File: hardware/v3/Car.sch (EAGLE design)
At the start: 56 parts, among them IC1 PIC24FJ64GB204

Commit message: Started layout for v3.
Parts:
- removed 3V3: LM317, misc:LM317
- removed C1: 10u, rcl:C-USC1206
- removed C2, C3, C4, C5, PSB3: 100n, rcl:C-USC0805
- removed C7, PSB2: 1u, rcl:C-USC1206
- removed PSB1: 100u, SparkFun-Passives:CAP_POLC
- removed R15: 240, rcl:R-US_R0805
- removed R16: 390, rcl:R-US_R0805
- removed RL1, RL2: 2k, rcl:R-US_R0805
- removed RN1: 10k, rcl:R-US_R0805
- added C11: 100u, SparkFun-Passives:CAP_POLC
- added C12, C14, C16, C21: 10u, rcl:C-USC1206
- added C13, C15, C17, C22, C23, C24, C41: 100n, rcl:C-USC0805
- added CN1: (no value), SmslsTron-1:USBMINIB
- added D1: (no value), SmslsTron-1:SCHOTTKY-DIODESMA
- added IC2: LD117AS50TR, v-reg:LD117AS50TR
- added IC3: LD117AS33TR, v-reg:LD117AS33TR
- added JP5: (no value), SmslsTron-1:PINHD-1X4
- added R11, R22: 2k, rcl:R-US_R0805
- added R21: 10k, rcl:R-US_R0805
- added R23, R25: 1k, rcl:R-US_R0805
- added R24, R26: 100, rcl:R-US_R0805
- added S1: SWITCH-MOMENTARY-2SMD-4, SmslsTron-1:SWITCH-MOMENTARY-2SMD-4
- added T1, T2: (no value), SmslsTron-1:NPNSOT23
- added U$1: FUSE24X06, SmslsTron-1:FUSE24X06
- 11RS, 12RS, 21RS, 22RS: device resistor:R-US_R2512 -> resistor:R-US_R1210
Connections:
- removed net 12V: 1LDB.1, 1LDC.+, 2LDB.1, 2LDC.+, 3V3.VI, J1.1, MD1.VLOAD, MD2.VLOAD, PSB1.+, PSB2.1, PSB3.1
- removed net 3V3: 3V3.VO, C2.1, C3.1, C4.1, C5.1, C7.1, IC1.AVDD, IC1.VBAT, IC1.VDD@1, IC1.VDD@2, IC1.VUSB3V3, ICD.2, JP2.4, MOUTH.VCC, PWR.A, R15.2, RN1.1
- removed net 5V: 1LGB.1, 2LGB.1, MD1.VLOGIC, MD2.VLOGIC
- removed net A7: HB.A
- removed net D12/M2_P1: MD2.PHASE1
- removed net D13/M2_P2: MD2.PHASE2
- removed net D13/SCK: JP4.6
- removed net D14/M2_I0X: MD2.I01, MD2.I02
- removed net D15/M2_I1X: MD2.I11, MD2.I12
- removed net D4/M1_P2: MD1.PHASE2
- removed net D7/M1_I0X: MD1.I01, MD1.I02
- removed net D8/M1_I1X: MD1.I11, MD1.I12
- removed net DGND: MD1.GND1, MD1.GND2, MD1.GND3, MD1.GND4, MD2.GND1, MD2.GND2, MD2.GND3, MD2.GND4
- removed net M1_I00: IC1.SOSCO/SC0/RA4
- removed net M1_I10: IC1.TDO/CN34/RA8
- removed net M1_V1: MD1.VREF1
- removed net M1_V2: MD1.VREF2
- removed net M2_I00: IC1.TMS/CN36/RA10
- removed net M2_I10: IC1.AN11/RP17/CN9/RC1
- removed net M2_V1: MD2.VREF1
- removed net M2_V2: MD2.VREF2
- removed net MISO: MOUTH.SDO
- removed net MOSI: MOUTH.SDI
- removed net SCLK: MOUTH.SCLK
- new net +3V3: C16.1, C17.1, C22.1, C23.1, C24.1, C41.1, IC1.AVDD, IC1.VBAT, IC1.VDD@1, IC1.VDD@2, IC1.VUSB3V3, IC3.OUT, ICD.2, JP2.4, MOUTH.VCC, PWR.A, R21.1
- new net +5V: 1LGB.1, 2LGB.1, C14.1, C15.1, IC2.OUT, IC3.IN, JP2.5, JP5.1, MD1.VLOGIC, MD2.VLOGIC, R24.2, R26.2
- new net A4_PO: JP5.2, T1.E
- new net A5_PO: JP5.3, T2.E
- new net M1_I02: IC1.TDO/CN34/RA8, MD1.I02
- new net M1_I12: IC1.TDI/CN35/RA9, MD1.I12
- new net M2_I02: IC1.CN24/VBUS/RB6, MD2.I02
- new net M2_I12: IC1.RP7/CN23/RB7, MD2.I12
- new net N$12: R26.1, T2.C
- new net N$19: R23.2, T1.B
- new net N$3: D1.A, U$1.2
- new net N$7: R24.1, T1.C
- new net VIN_PRF: J1.1, U$1.1
- net /RST: now also R21.2, S1.1; no longer RN1.2
- net A4: now also R23.1
- net A5: now also R25.1
- net D10/M2_PWM2: now also MD2.VREF2
- net D11/MOSI: now also MOUTH.SDI
- net D12/MISO: now also MOUTH.SDO
- net D13/SCLK: now also HB.A, JP4.6, MOUTH.SCLK
- net D3/M1_P2: now also MD1.PHASE2
- net D4/M2_P1: now also MD2.PHASE1
- net D5/M1_PWM1: now also MD1.VREF1
- net D6/M1_PWM2: now also MD1.VREF2
- net D7/M2_P2: now also MD2.PHASE2
- net D9/M2_PWM1: now also MD2.VREF1
- net GND: now also C11.-, C12.2, C13.2, C14.2, C15.2, C16.2, C17.2, C21.2, C22.2, C23.2, C24.2, C41.2, IC2.ADJ, IC3.ADJ, JP5.4, MD1.GND1, MD1.GND2, MD1.GND3, MD1.GND4, MD2.GND1, MD2.GND2, MD2.GND3, MD2.GND4, R11.2, R22.2, S1.2; no longer C1.2, C2.2, C3.2, C4.2, C5.2, C7.2, PSB1.-, PSB2.2, PSB3.2, R16.1, RL1.2, RL2.2
- net M1_I01: now also IC1.SOSCO/SC0/RA4, MD1.I01; no longer IC1.TCK/CN33/RA7
- net M1_I11: now also IC1.TCK/CN33/RA7, MD1.I11; no longer IC1.TDI/CN35/RA9
- net M2_I01: now also IC1.TMS/CN36/RA10, MD2.I01; no longer IC1.AN9/RP15/CN11/RB15
- net M2_I11: now also IC1.AN9/RP15/CN11/RB15, MD2.I11; no longer IC1.AN12/RP18/CN10/RC2
- net N$20: now also R25.2, T2.B; no longer 3V3.ADJ, R15.1, R16.2
- net N$40: now also C21.1, IC1.VCAP; no longer C1.1
- net N$46: now also R22.1; no longer RL1.1
- net N$65: now also R11.1; no longer RL2.1
- net RFM_CS: now also IC1.AN12/RP18/CN10/RC2; no longer IC1.RP7/CN23/RB7
- net RFM_IRQ: now also IC1.AN11/RP17/CN9/RC1; no longer IC1.CN24/VBUS/RB6
- net VIN: now also 1LDB.1, 1LDC.+, 2LDB.1, 2LDC.+, C11.+, C12.1, C13.1, D1.C, IC2.IN, MD1.VLOAD, MD2.VLOAD

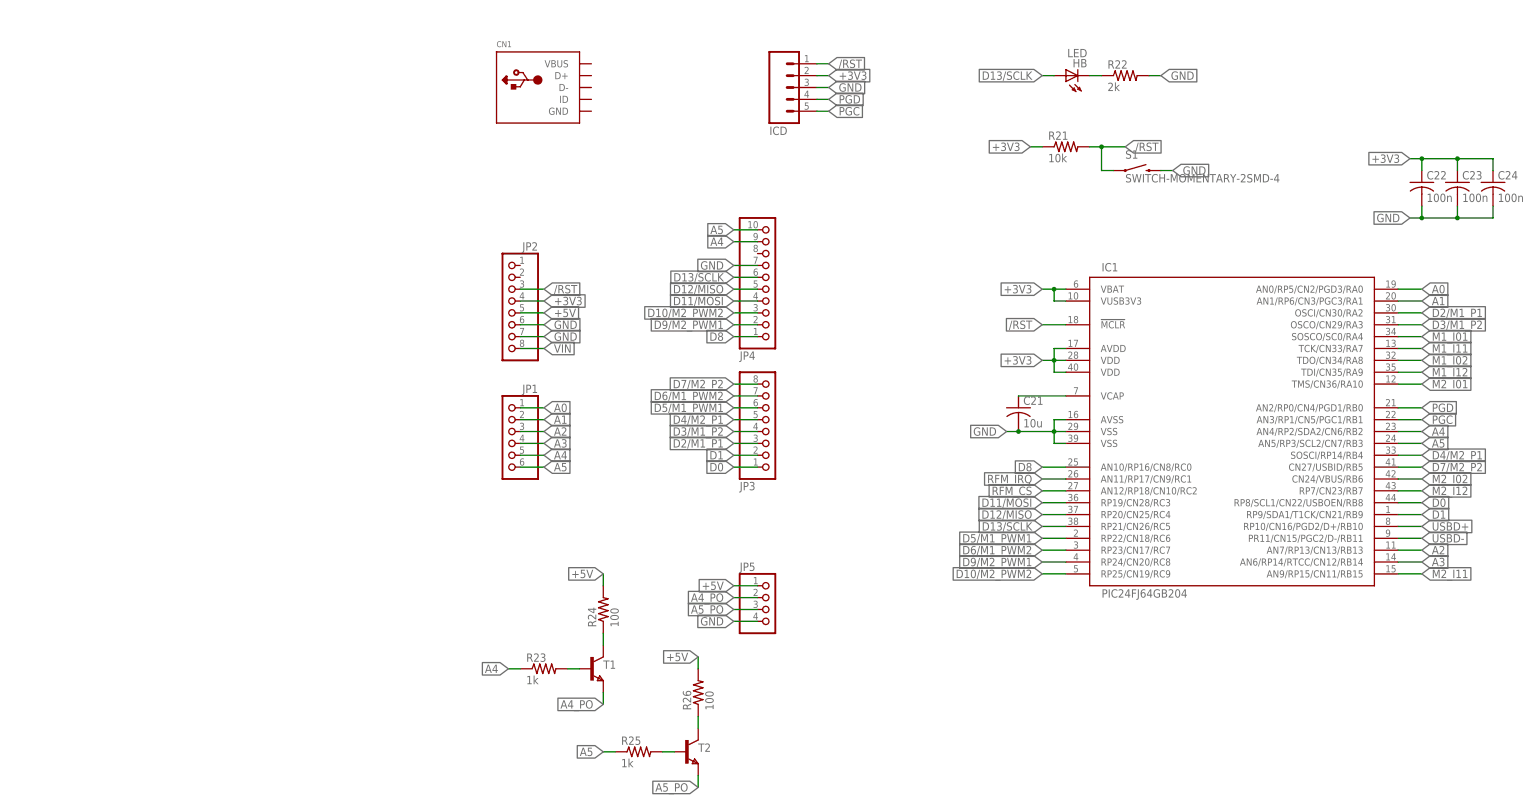
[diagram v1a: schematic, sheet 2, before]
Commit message: Continued working layout. Added USB components. Remapped some pins.
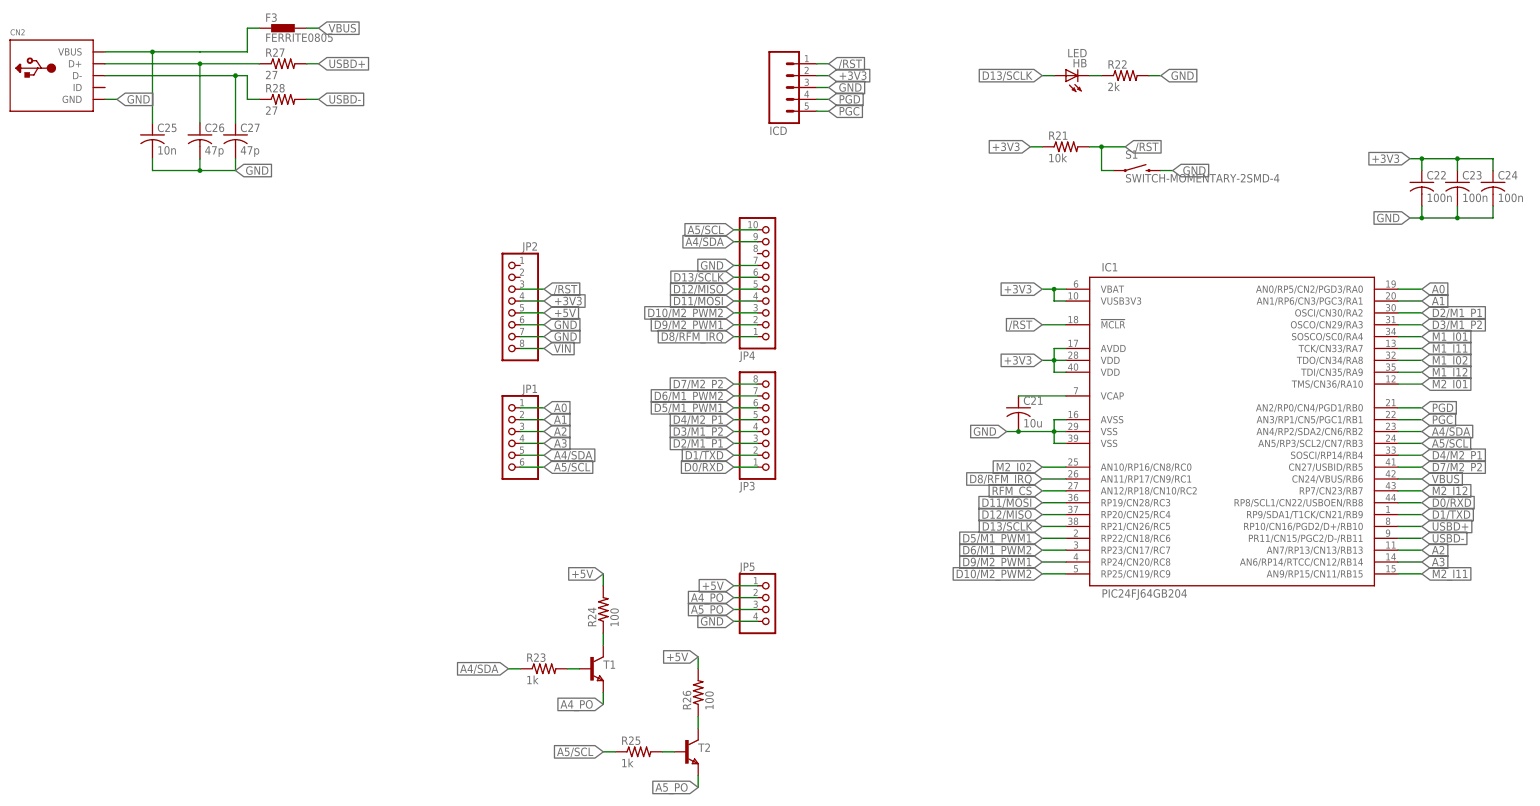
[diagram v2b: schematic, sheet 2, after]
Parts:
- removed CN1: (no value), SmslsTron-1:USBMINIB
- added C25: 10n, rcl:C-USC0805
- added C26, C27: 47p, rcl:C-USC0805
- added CN2: (no value), adafruit:USBMINIB
- added F3: FERRITE0805, SMSLS:FERRITE0805
- added R27, R28: 27, resistor:R-US_R0805
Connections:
- net A4 renamed A4/SDA
- net A5 renamed A5/SCL
- net D0 renamed D0/RXD
- net D1 renamed D1/TXD
- removed net D8: IC1.AN10/RP16/CN8/RC0, JP4.1
- removed net RFM_IRQ: IC1.AN11/RP17/CN9/RC1, MOUTH.NIRQ
- new net D8/RFM_IRQ: IC1.AN11/RP17/CN9/RC1, JP4.1, MOUTH.NIRQ
- new net N$21: C26.1, CN2.D+, R27.1
- new net N$22: C27.1, CN2.D-, R28.1
- new net VBUS: F3.2, IC1.CN24/VBUS/RB6
- new net VBUS-PRF: C25.1, CN2.VBUS, F3.1
- net GND: now also C25.2, C26.2, C27.2, CN2.GND
- net M2_I02: now also IC1.AN10/RP16/CN8/RC0; no longer IC1.CN24/VBUS/RB6
- net USBD+: now also R27.2
- net USBD-: now also R28.2

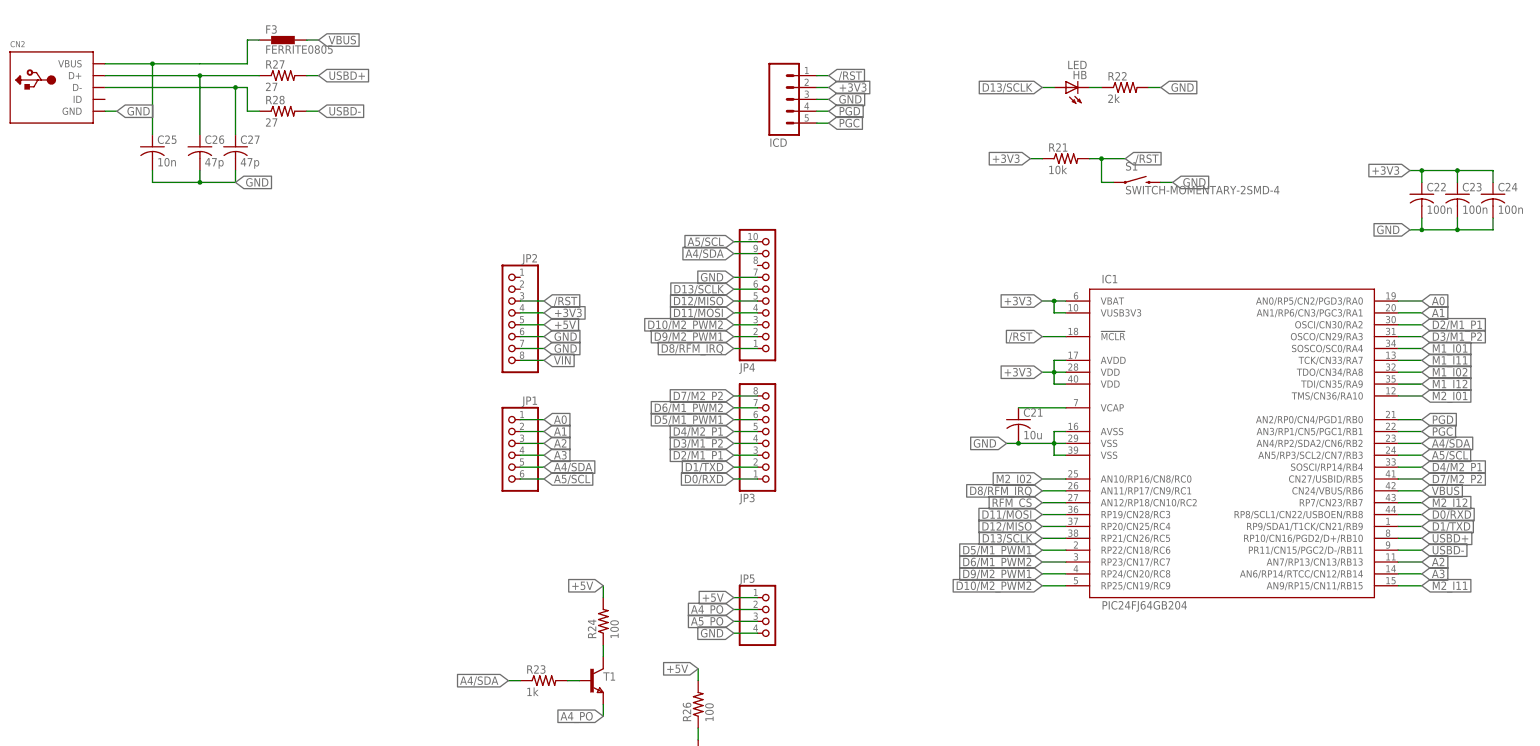
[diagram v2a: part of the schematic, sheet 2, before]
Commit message: More routing (~50% complete). Normalized/placed texts.
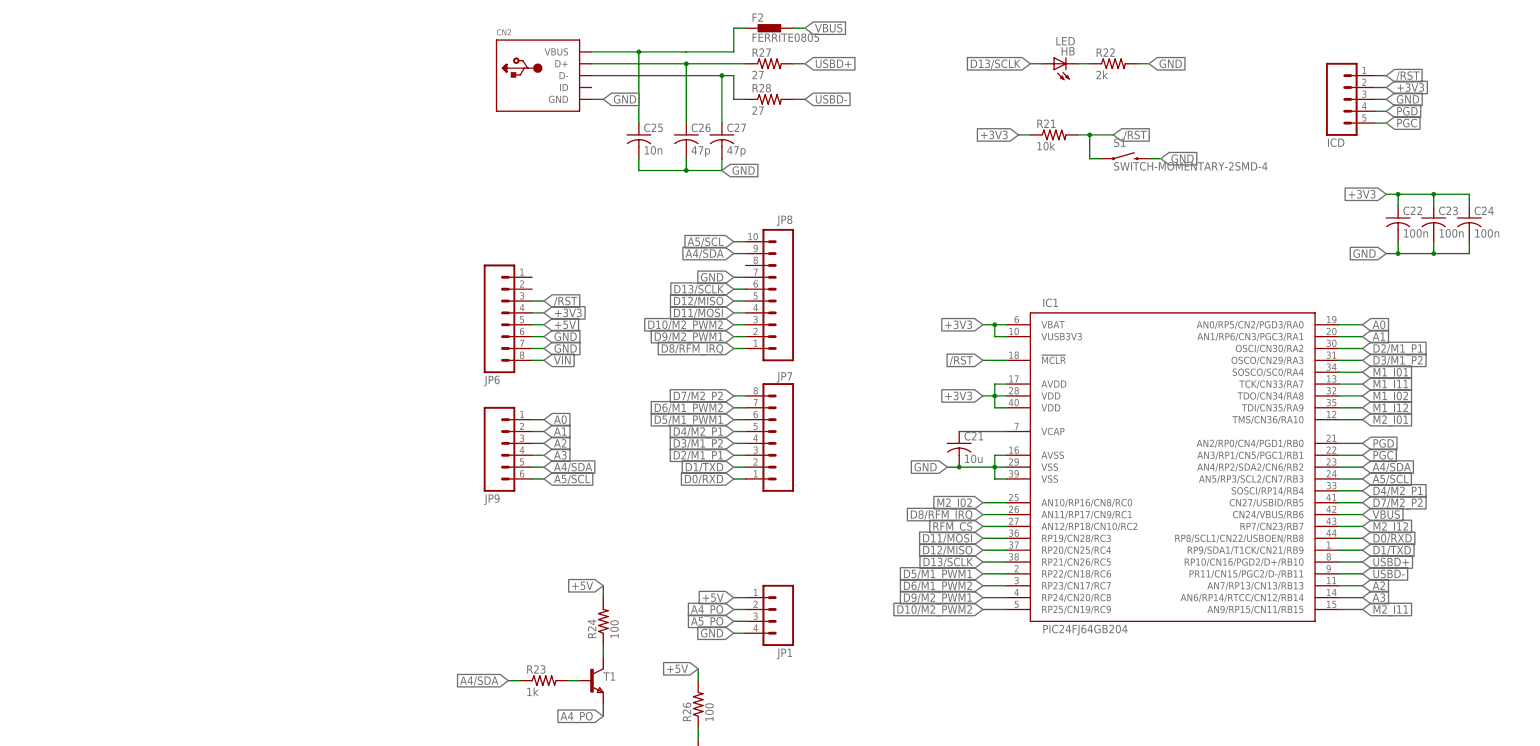
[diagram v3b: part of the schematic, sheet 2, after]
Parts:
- removed F3: FERRITE0805, SMSLS:FERRITE0805
- removed JP2, JP3: (no value), pinhead:PINHD-1X8
- removed JP4: (no value), pinhead:PINHD-1X10
- removed JP5: (no value), SmslsTron-1:PINHD-1X4
- added F2: FERRITE0805, SMSLS:FERRITE0805
- added JP6, JP7: (no value), SparkFun-Connectors:M08LOCK
- added JP8: (no value), SparkFun-Connectors:M10LOCK
- added JP9: (no value), SparkFun-Connectors:M06LOCK
- JP1: device pinhead:PINHD-1X6 -> SparkFun-Connectors:M04LOCK
- M1, M2: device SparkFun-Connectors:M04LOCK_LONGPADS -> SparkFun-Connectors:M04LOCK
- renumbered U$1 to F1
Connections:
- net +3V3: now also JP6.4; no longer JP2.4
- net +5V: now also JP1.1, JP6.5; no longer JP2.5, JP5.1
- net /RST: now also JP6.3; no longer JP2.3
- net A0: now also JP9.1; no longer JP1.1
- net A1: now also JP9.2; no longer JP1.2
- net A2: now also JP9.3; no longer JP1.3
- net A3: now also JP9.4; no longer JP1.4
- net A4/SDA: now also JP8.9, JP9.5; no longer JP1.5, JP4.9
- net A4_PO: now also JP1.2; no longer JP5.2
- net A5/SCL: now also JP8.10, JP9.6; no longer JP1.6, JP4.10
- net A5_PO: now also JP1.3; no longer JP5.3
- net D0/RXD: now also JP7.1; no longer JP3.1
- net D1/TXD: now also JP7.2; no longer JP3.2
- net D10/M2_PWM2: now also JP8.3; no longer JP4.3
- net D11/MOSI: now also JP8.4; no longer JP4.4
- net D12/MISO: now also JP8.5; no longer JP4.5
- net D13/SCLK: now also JP8.6; no longer JP4.6
- net D2/M1_P1: now also JP7.3; no longer JP3.3
- net D3/M1_P2: now also JP7.4; no longer JP3.4
- net D4/M2_P1: now also JP7.5; no longer JP3.5
- net D5/M1_PWM1: now also JP7.6; no longer JP3.6
- net D6/M1_PWM2: now also JP7.7; no longer JP3.7
- net D7/M2_P2: now also JP7.8; no longer JP3.8
- net D8/RFM_IRQ: now also JP8.1; no longer JP4.1
- net D9/M2_PWM1: now also JP8.2; no longer JP4.2
- net GND: now also JP1.4, JP6.6, JP6.7, JP8.7; no longer JP2.6, JP2.7, JP4.7, JP5.4
- net VBUS: now also F2.2; no longer F3.2
- net VBUS-PRF: now also F2.1; no longer F3.1
- net VIN: now also JP6.8; no longer JP2.8
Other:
- moved on the sheet: C21, C22, C23, C24, C25, C26, C27, CN2, HB, IC1, ICD, R21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
